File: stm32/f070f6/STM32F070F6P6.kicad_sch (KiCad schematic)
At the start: 29 parts, among them J1 STLINK, J3 L, J3 USB_C_REC_16PIN, J4 L, SW1 BOOT0, U1 XC6220B331MR, U2 STM32F070F6Px, Y1 8 MHz

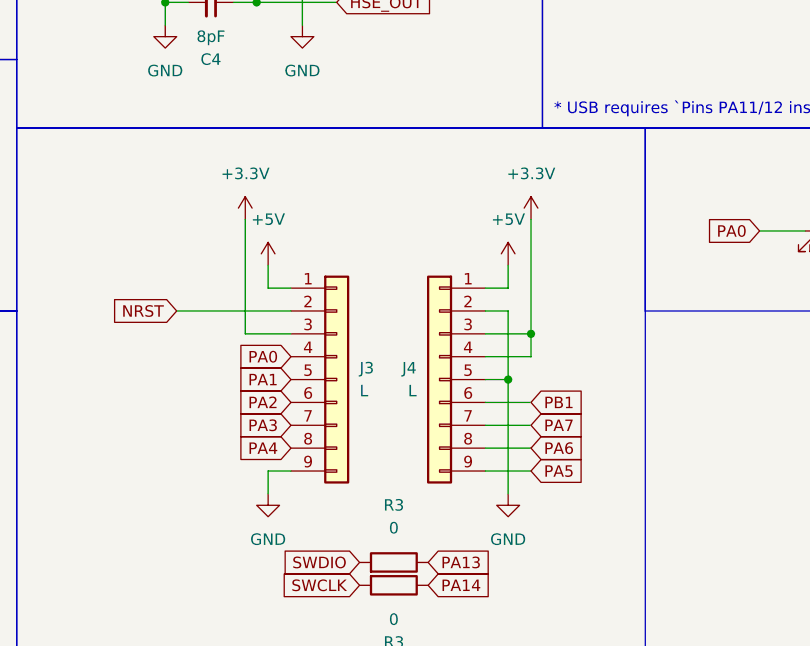
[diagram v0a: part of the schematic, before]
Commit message: Changed `9-Pin` header to 8 pin header.
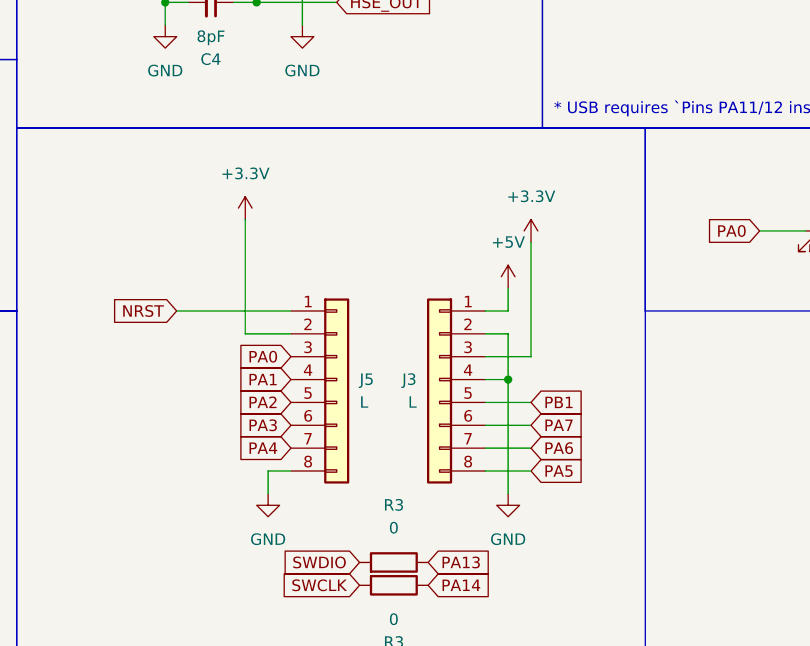
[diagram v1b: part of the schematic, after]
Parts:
- removed J3, J4: L, Connector_PinHeader_2.54mm:PinHeader_1x09_P2.54mm_Vertical, symbol Connector_Generic:Conn_01x09
- added J3, J5: L, Connector_PinHeader_2.54mm:PinHeader_1x08_P2.54mm_Vertical, symbol Connector_Generic:Conn_01x08
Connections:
- net +3.3V: now also J3.3 (Pin_3), J5.2 (Pin_2)
- net +5V: now also J3.1 (Pin_1)
- net GND: now also J3.2 (Pin_2), J3.4 (Pin_4), J5.8 (Pin_8)
- net NRST: now also J5.1 (Pin_1)
- net PA0: now also J5.3 (Pin_3)
- net PA1: now also J5.4 (Pin_4)
- net PA2: now also J5.5 (Pin_5)
- net PA3: now also J5.6 (Pin_6)
- net PA4: now also J5.7 (Pin_7)
- net PA5: now also J3.8 (Pin_8)
- net PA6: now also J3.7 (Pin_7)
- net PA7: now also J3.6 (Pin_6)
- net PB1: now also J3.5 (Pin_5)

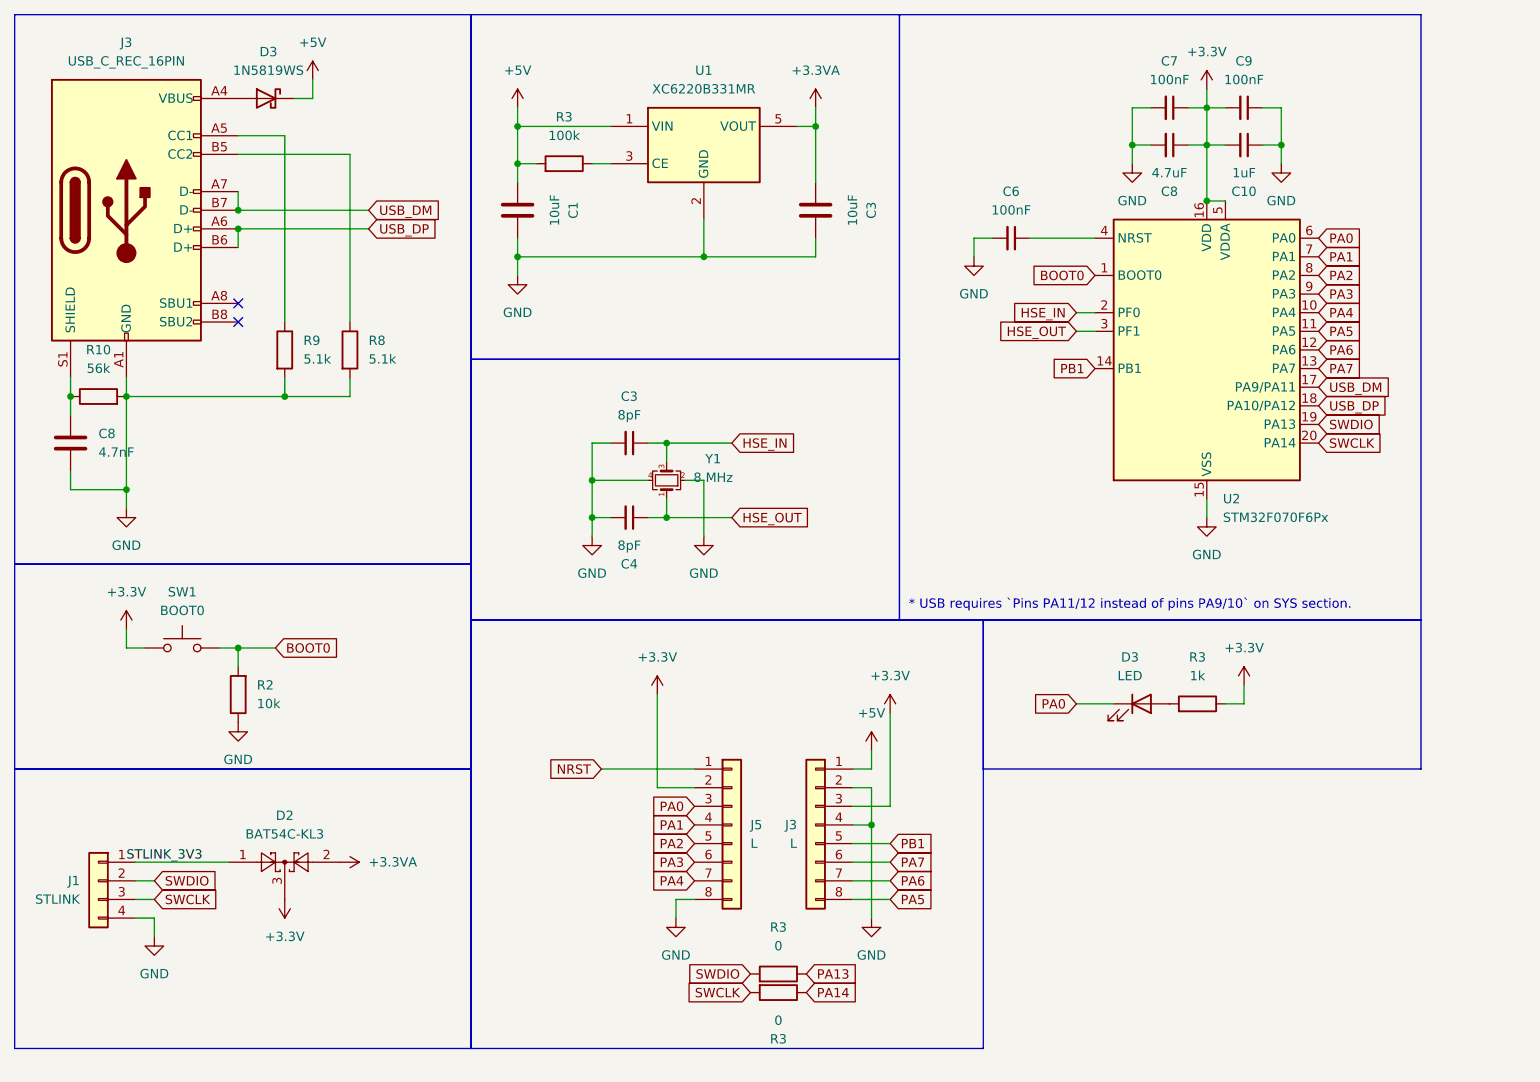
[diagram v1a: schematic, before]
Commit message: Update: Artwork completed for `F070F6P6`.
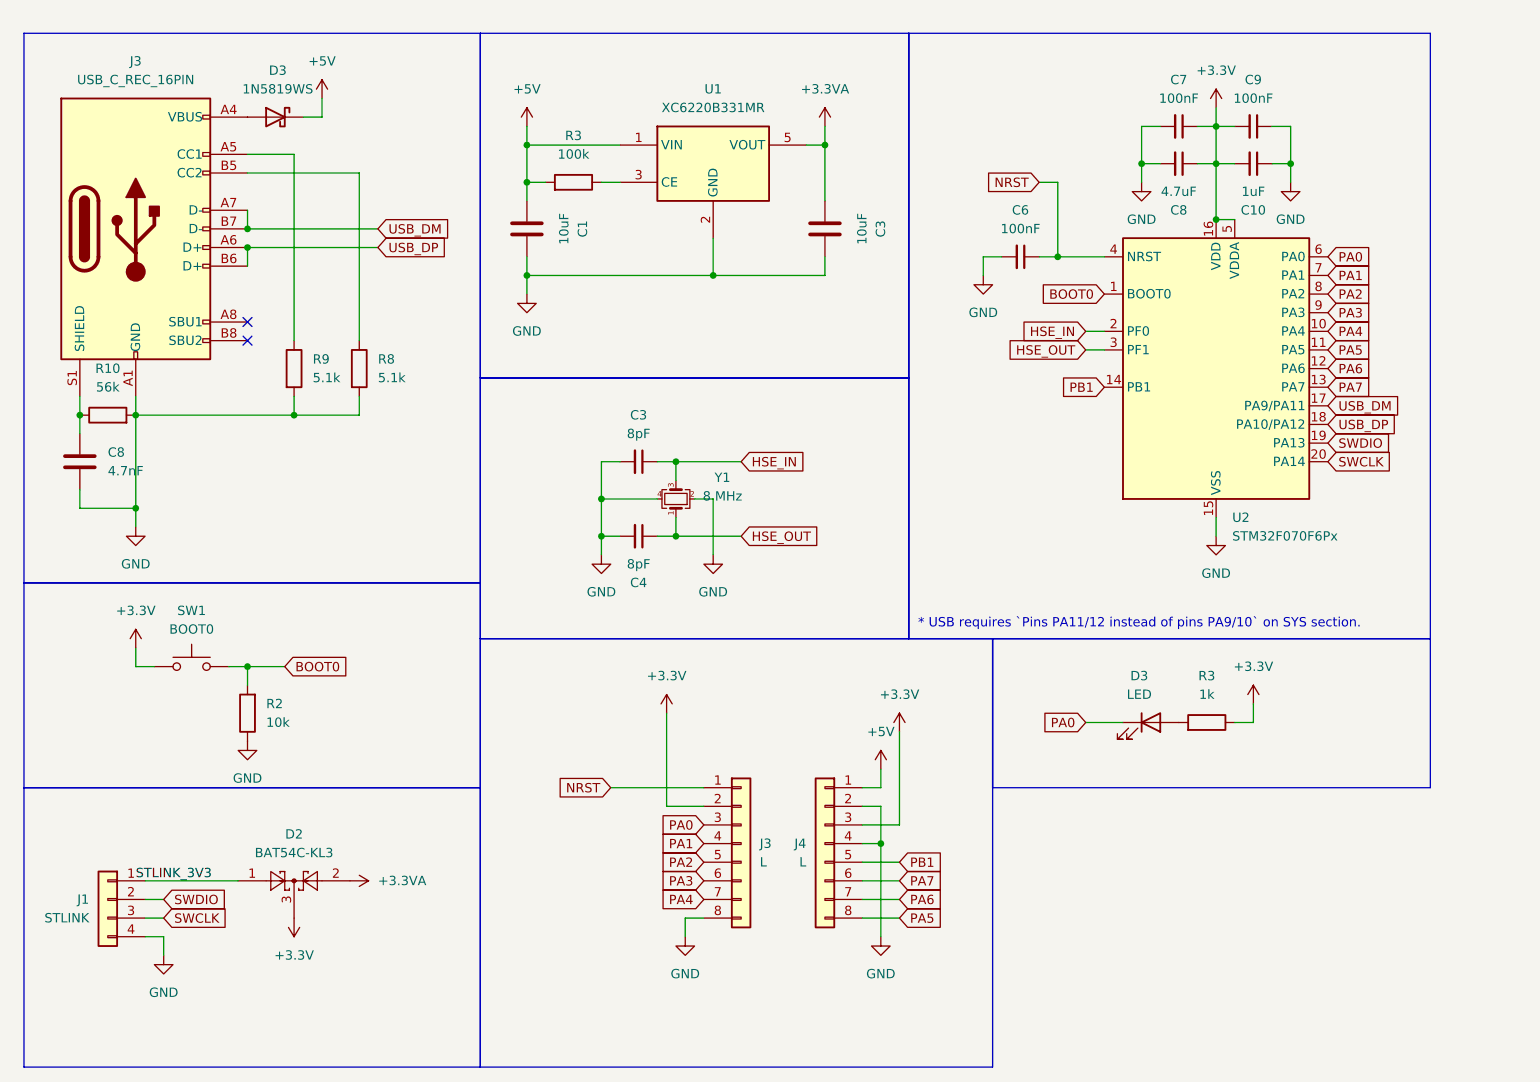
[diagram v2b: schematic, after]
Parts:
- removed J5: L, Connector_PinHeader_2.54mm:PinHeader_1x08_P2.54mm_Vertical, symbol Connector_Generic:Conn_01x08
- removed R3: 100k, Resistor_SMD:R_0603_1608Metric, symbol Device:R
- removed R3: 1k, Resistor_SMD:R_0603_1608Metric, symbol Device:R
- removed R3 (x2): 0, Resistor_SMD:R_0603_1608Metric, symbol Device:R
- added J4: L, Connector_PinHeader_2.54mm:PinHeader_1x08_P2.54mm_Vertical, symbol Connector_Generic:Conn_01x08
- added R3: 100k, Resistor_SMD:R_0603_1608Metric, symbol Device:R
- added R3: 1k, Resistor_SMD:R_0603_1608Metric, symbol Device:R
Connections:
- net +3.3V: now also J3.2 (Pin_2), J4.3 (Pin_3), R3.1; no longer J3.3 (Pin_3)
- net +5V: now also J4.1 (Pin_1), R3.2; no longer J3.1 (Pin_1)
- net GND: now also J3.8 (Pin_8), J4.2 (Pin_2), J4.4 (Pin_4); no longer J3.2 (Pin_2), J3.4 (Pin_4)
- net NRST: now also C6.1, J3.1 (Pin_1), U2.4 (NRST)
- net PA0: now also J3.3 (Pin_3)
- net PA1: now also J3.4 (Pin_4)
- net PA2: now also J3.5 (Pin_5)
- net PA3: now also J3.6 (Pin_6)
- net PA4: now also J3.7 (Pin_7)
- net PA5: now also J4.8 (Pin_8); no longer J3.8 (Pin_8)
- net PA6: now also J4.7 (Pin_7); no longer J3.7 (Pin_7)
- net PA7: now also J4.6 (Pin_6); no longer J3.6 (Pin_6)
- net PB1: now also J4.5 (Pin_5); no longer J3.5 (Pin_5)
- net at U1.3 (CE): now also R3.1
- net at D3.2 (A): now also R3.2

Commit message: Update 2023-11-27
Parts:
- removed J3, J4: L, Connector_PinHeader_2.54mm:PinHeader_1x08_P2.54mm_Vertical, symbol Connector_Generic:Conn_01x08
- added J3, J4: L, Connector_PinSocket_2.54mm:PinSocket_1x10_P2.54mm_Vertical, symbol Connector_Generic:Conn_01x10
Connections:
- net +3.3V: now also J3.1 (Pin_1), J3.4 (Pin_4), J4.4 (Pin_4), J4.9 (Pin_9)
- net +5V: now also J4.1 (Pin_1), J4.2 (Pin_2)
- net BOOT0: now also J3.2 (Pin_2)
- net GND: now also J3.10 (Pin_10), J4.10 (Pin_10), J4.3 (Pin_3)
- net NRST: now also J3.3 (Pin_3)
- net PA0: now also J3.5 (Pin_5)
- net PA1: now also J3.6 (Pin_6)
- net PA2: now also J3.7 (Pin_7)
- net PA3: now also J3.8 (Pin_8)
- net PA4: now also J3.9 (Pin_9)
- net PA5: now also J4.8 (Pin_8)
- net PA6: now also J4.7 (Pin_7)
- net PA7: now also J4.6 (Pin_6)
- net PB1: now also J4.5 (Pin_5)
